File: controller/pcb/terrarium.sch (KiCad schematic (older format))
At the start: 54 parts, among them Q1 S8050, Q2 S8050, Q3 S8050, SW1 SW_Push, SW2 SW_Push, U1 ESP32-WROOM-32, U2 DS3231M, U3 LM1117-3.3

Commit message: pcb: developing smd layout
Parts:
- D1, D2, D3: footprint Diode_THT:D_DO-41_SOD81_P7.62mm_Horizontal -> Diode_SMD:D_1206_3216Metric
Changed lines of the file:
@@
 F 0 "D1" V 7350 1600 50  0000 L CNN
 F 1 "1N47xxA" H 7200 1450 50  0000 L CNN
-F 2 "Diode_THT:D_DO-41_SOD81_P7.62mm_Horizontal" H 7350 1375 50  0001 C CNN
+F 2 "Diode_SMD:D_1206_3216Metric" H 7350 1375 50  0001 C CNN
 F 3 "https://www.vishay.com/docs/85816/1n4728a.pdf" H 7350 1550 50  0001 C CNN
 	1    7350 1550
@@
 F 0 "D2" V 7350 3200 50  0000 L CNN
 F 1 "1N47xxA" H 7200 3050 50  0000 L CNN
-F 2 "Diode_THT:D_DO-41_SOD81_P7.62mm_Horizontal" H 7350 2975 50  0001 C CNN
+F 2 "Diode_SMD:D_1206_3216Metric" H 7350 2975 50  0001 C CNN
 F 3 "https://www.vishay.com/docs/85816/1n4728a.pdf" H 7350 3150 50  0001 C CNN
 	1    7350 3150
@@
 F 0 "D3" V 7350 4750 50  0000 L CNN
 F 1 "1N47xxA" H 7200 4600 50  0000 L CNN
-F 2 "Diode_THT:D_DO-41_SOD81_P7.62mm_Horizontal" H 7350 4525 50  0001 C CNN
+F 2 "Diode_SMD:D_1206_3216Metric" H 7350 4525 50  0001 C CNN
 F 3 "https://www.vishay.com/docs/85816/1n4728a.pdf" H 7350 4700 50  0001 C CNN
 	1    7350 4700

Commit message: Add copper plate, minor changes
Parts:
- H1, H2, H3, H4: footprint MountingHole:MountingHole_3.2mm_M3_DIN965_Pad -> MountingHole:MountingHole_3.2mm_M3_Pad_Via
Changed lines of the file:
@@
 F 0 "H1" H 3500 3500 50  0000 L CNN
 F 1 "MountingHole" H 3500 3455 50  0001 L CNN
-F 2 "MountingHole:MountingHole_3.2mm_M3_DIN965_Pad" H 3400 3500 50  0001 C CNN
+F 2 "MountingHole:MountingHole_3.2mm_M3_Pad_Via" H 3400 3500 50  0001 C CNN
 F 3 "~" H 3400 3500 50  0001 C CNN
 	1    3400 3500
@@
 F 0 "H2" H 3900 3500 50  0000 L CNN
 F 1 "MountingHole" H 3900 3455 50  0001 L CNN
-F 2 "MountingHole:MountingHole_3.2mm_M3_DIN965_Pad" H 3800 3500 50  0001 C CNN
+F 2 "MountingHole:MountingHole_3.2mm_M3_Pad_Via" H 3800 3500 50  0001 C CNN
 F 3 "~" H 3800 3500 50  0001 C CNN
 	1    3800 3500
@@
 F 0 "H3" H 3500 3800 50  0000 L CNN
 F 1 "MountingHole" H 3500 3755 50  0001 L CNN
-F 2 "MountingHole:MountingHole_3.2mm_M3_DIN965_Pad" H 3400 3800 50  0001 C CNN
+F 2 "MountingHole:MountingHole_3.2mm_M3_Pad_Via" H 3400 3800 50  0001 C CNN
 F 3 "~" H 3400 3800 50  0001 C CNN
 	1    3400 3800
@@
 F 0 "H4" H 3900 3800 50  0000 L CNN
 F 1 "MountingHole" H 3900 3755 50  0001 L CNN
-F 2 "MountingHole:MountingHole_3.2mm_M3_DIN965_Pad" H 3800 3800 50  0001 C CNN
+F 2 "MountingHole:MountingHole_3.2mm_M3_Pad_Via" H 3800 3800 50  0001 C CNN
 F 3 "~" H 3800 3800 50  0001 C CNN
 	1    3800 3800

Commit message: pcb updates
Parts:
- SW1: value SW_Push -> RESET
- SW2: value SW_Push -> BOOT
- renumbered CONN1 to UART1
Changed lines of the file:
@@
 P 14950 1600
 F 0 "SW2" H 14950 1885 50  0000 C CNN
-F 1 "SW_Push" H 14950 1794 50  0000 C CNN
+F 1 "BOOT" H 14950 1794 50  0000 C CNN
 F 2 "Button_Switch_SMD:SW_DIP_SPSTx01_Slide_6.7x4.1mm_W6.73mm_P2.54mm_LowProfile_JPin" H 14950 1800 50  0001 C CNN
 F 3 "~" H 14950 1800 50  0001 C CNN
@@
 P 11950 1600
 F 0 "SW1" H 11950 1885 50  0000 C CNN
-F 1 "SW_Push" H 11950 1794 50  0000 C CNN
+F 1 "RESET" H 11950 1794 50  0000 C CNN
 F 2 "Button_Switch_SMD:SW_DIP_SPSTx01_Slide_6.7x4.1mm_W6.73mm_P2.54mm_LowProfile_JPin" H 11950 1800 50  0001 C CNN
 F 3 "~" H 11950 1800 50  0001 C CNN
@@
 $EndComp
 $Comp
-L Connector_Generic:Conn_01x04 CONN1
+L Connector_Generic:Conn_01x04 UART1
 U 1 1 61BD0ED7
 P 12500 3700
-F 0 "CONN1" H 12580 3692 50  0000 L CNN
-F 1 "data" H 12580 3601 50  0000 L CNN
+F 0 "UART1" H 12580 3692 50  0000 L CNN
+F 1 "data" H 12650 3100 50  0001 L CNN
 F 2 "Connector_PinHeader_2.54mm:PinHeader_1x04_P2.54mm_Vertical" H 12500 3700 50  0001 C CNN
 F 3 "~" H 12500 3700 50  0001 C CNN

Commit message: pcb: updates
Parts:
- added D4: 1N47xxA, Diode_SMD:D_1206_3216Metric, symbol Diode:1N47xxA
- added SW3: RESET RTC, Button_Switch_SMD:SW_DIP_SPSTx01_Slide_6.7x4.1mm_W6.73mm_P2.54mm_LowProfile_JPin, symbol Switch:SW_Push
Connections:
- wire segments 169 -> 171
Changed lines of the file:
@@
 $EndComp
 Wire Wire Line
-	3250 8300 3250 7800
-Wire Wire Line
-	2350 7800 3250 7800
+	3250 8300 3250 8250
+Wire Wire Line
+	2350 7800 2650 7800
 Wire Wire Line
 	3250 8600 3250 9050
@@
 	1    0    0    -1
 $EndComp
+$Comp
+L Diode:1N47xxA D4
+U 1 1 61C05BEB
+P 2800 7800
+F 0 "D4" H 2750 7900 50  0000 L CNN
+F 1 "1N47xxA" H 2650 7700 50  0000 L CNN
+F 2 "Diode_SMD:D_1206_3216Metric" H 2800 7625 50  0001 C CNN
+F 3 "https://www.vishay.com/docs/85816/1n4728a.pdf" H 2800 7800 50  0001 C CNN
+	1    2800 7800
+	1    0    0    -1
+$EndComp
+Wire Wire Line
+	2950 7800 3250 7800
+$Comp
+L Switch:SW_Push SW3
+U 1 1 61C4BD91
+P 3250 8050
+F 0 "SW3" H 3250 8335 50  0000 C CNN
+F 1 "RESET RTC" H 3250 8244 50  0000 C CNN
+F 2 "Button_Switch_SMD:SW_DIP_SPSTx01_Slide_6.7x4.1mm_W6.73mm_P2.54mm_LowProfile_JPin" H 3250 8250 50  0001 C CNN
+F 3 "~" H 3250 8250 50  0001 C CNN
+	1    3250 8050
+	0    1    1    0
+$EndComp
+Wire Wire Line
+	3250 7850 3250 7800
 $EndSCHEMATC

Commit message: pcb v1.3 finished
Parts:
- D1, D2, D3: value 1N47xxA -> M7; footprint Diode_SMD:D_1206_3216Metric -> Diode_SMD:D_2114_3652Metric
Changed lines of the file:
@@
 P 7350 1550
 F 0 "D1" V 7350 1600 50  0000 L CNN
-F 1 "1N47xxA" H 7200 1450 50  0000 L CNN
-F 2 "Diode_SMD:D_1206_3216Metric" H 7350 1375 50  0001 C CNN
+F 1 "M7" V 7350 1350 50  0000 L CNN
+F 2 "Diode_SMD:D_2114_3652Metric" H 7350 1375 50  0001 C CNN
 F 3 "https://www.vishay.com/docs/85816/1n4728a.pdf" H 7350 1550 50  0001 C CNN
 	1    7350 1550
@@
 P 7350 3150
 F 0 "D2" V 7350 3200 50  0000 L CNN
-F 1 "1N47xxA" H 7200 3050 50  0000 L CNN
-F 2 "Diode_SMD:D_1206_3216Metric" H 7350 2975 50  0001 C CNN
+F 1 "M7" V 7350 2950 50  0000 L CNN
+F 2 "Diode_SMD:D_2114_3652Metric" H 7350 2975 50  0001 C CNN
 F 3 "https://www.vishay.com/docs/85816/1n4728a.pdf" H 7350 3150 50  0001 C CNN
 	1    7350 3150
@@
 P 7350 4700
 F 0 "D3" V 7350 4750 50  0000 L CNN
-F 1 "1N47xxA" H 7200 4600 50  0000 L CNN
-F 2 "Diode_SMD:D_1206_3216Metric" H 7350 4525 50  0001 C CNN
+F 1 "M7" V 7350 4500 50  0000 L CNN
+F 2 "Diode_SMD:D_2114_3652Metric" H 7350 4525 50  0001 C CNN
 F 3 "https://www.vishay.com/docs/85816/1n4728a.pdf" H 7350 4700 50  0001 C CNN
 	1    7350 4700

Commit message: Pcb/v1.4 (#3)
* pcb: refactor

* minor updates, bjt to sot-23

* rtc charge, refactoring

* update jst footprints, added missing 3d models

* refactoring

* minor changes

* diode for battery

* fix bugs in UART

* add transistor for sensors

* move status led from relay circuit

* pcb v1.4 release

* fix snake logo

Co-authored-by: Grigorii Merkushev <brushknight@pop-os.localdomain>
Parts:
- removed Q1, Q2: S8050, Package_TO_SOT_THT:TO-92_Inline, symbol Transistor_BJT:S8050
- removed SW2: BOOT, Button_Switch_SMD:SW_DIP_SPSTx01_Slide_6.7x4.1mm_W6.73mm_P2.54mm_LowProfile_JPin, symbol Switch:SW_Push
- added LED5: SENS, LED_SMD:LED_1206_3216Metric, symbol Device:LED
- added Q1, Q2, Q4: S8050, Package_TO_SOT_SMD:SOT-23, symbol Device:Q_NPN_BEC
- added R13: 100k, Resistor_SMD:R_1206_3216Metric, symbol Device:R_Small
- added R14, R15, R16, R17: 5k, Resistor_SMD:R_1206_3216Metric, symbol Device:R_Small
- added RESET_j1: data, Connector_PinHeader_2.54mm:PinHeader_1x02_P2.54mm_Vertical, symbol Connector_Generic:Conn_01x02
- added TP1, TP2: TestPoint, TestPoint:TestPoint_Pad_1.5x1.5mm, symbol Connector:TestPoint
- D1, D2, D3: footprint Diode_SMD:D_2114_3652Metric -> Diode_SMD:D_2010_5025Metric
- D4: footprint Diode_SMD:D_1206_3216Metric -> Diode_SMD:D_2010_5025Metric
- Q3: footprint Package_TO_SOT_THT:TO-92_Inline -> Package_TO_SOT_SMD:SOT-23; symbol Transistor_BJT:S8050 -> Device:Q_NPN_BEC
- R10: value 10k -> 150ohm
- R12: value 300 -> 5k
- R2, R4, R6: value R_Small -> 10
- SW3: value RESET RTC -> RTC BATTERY
- UART1: footprint Connector_PinHeader_2.54mm:PinHeader_1x04_P2.54mm_Vertical -> Connector_PinHeader_2.54mm:PinHeader_1x06_P2.54mm_Vertical; symbol Connector_Generic:Conn_01x04 -> Connector_Generic:Conn_01x06
- renumbered HT1 to SENS1, HT2 to SENS2, HT3 to SENS3, HT4 to SENS4, HT5 to SENS5, HT6 to SENS6
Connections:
- net labels added: EN, G32, G33, IO0
- wire segments 171 -> 192
- no-connect marks 30 -> 28
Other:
- note added: "DS3231 rtc"
- note added: "ESP32 WROOM 32"
- note added: "Power 3v3 and 5v"
- note added: "Sensors"
- note added: "Status LED"
- note removed: "DHT22 sensors"
- note removed: "Utils"
- moved on the sheet: ALED1, BT1, C1, C2, C3, D1, D2, D3, D4, H1, H2, H3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

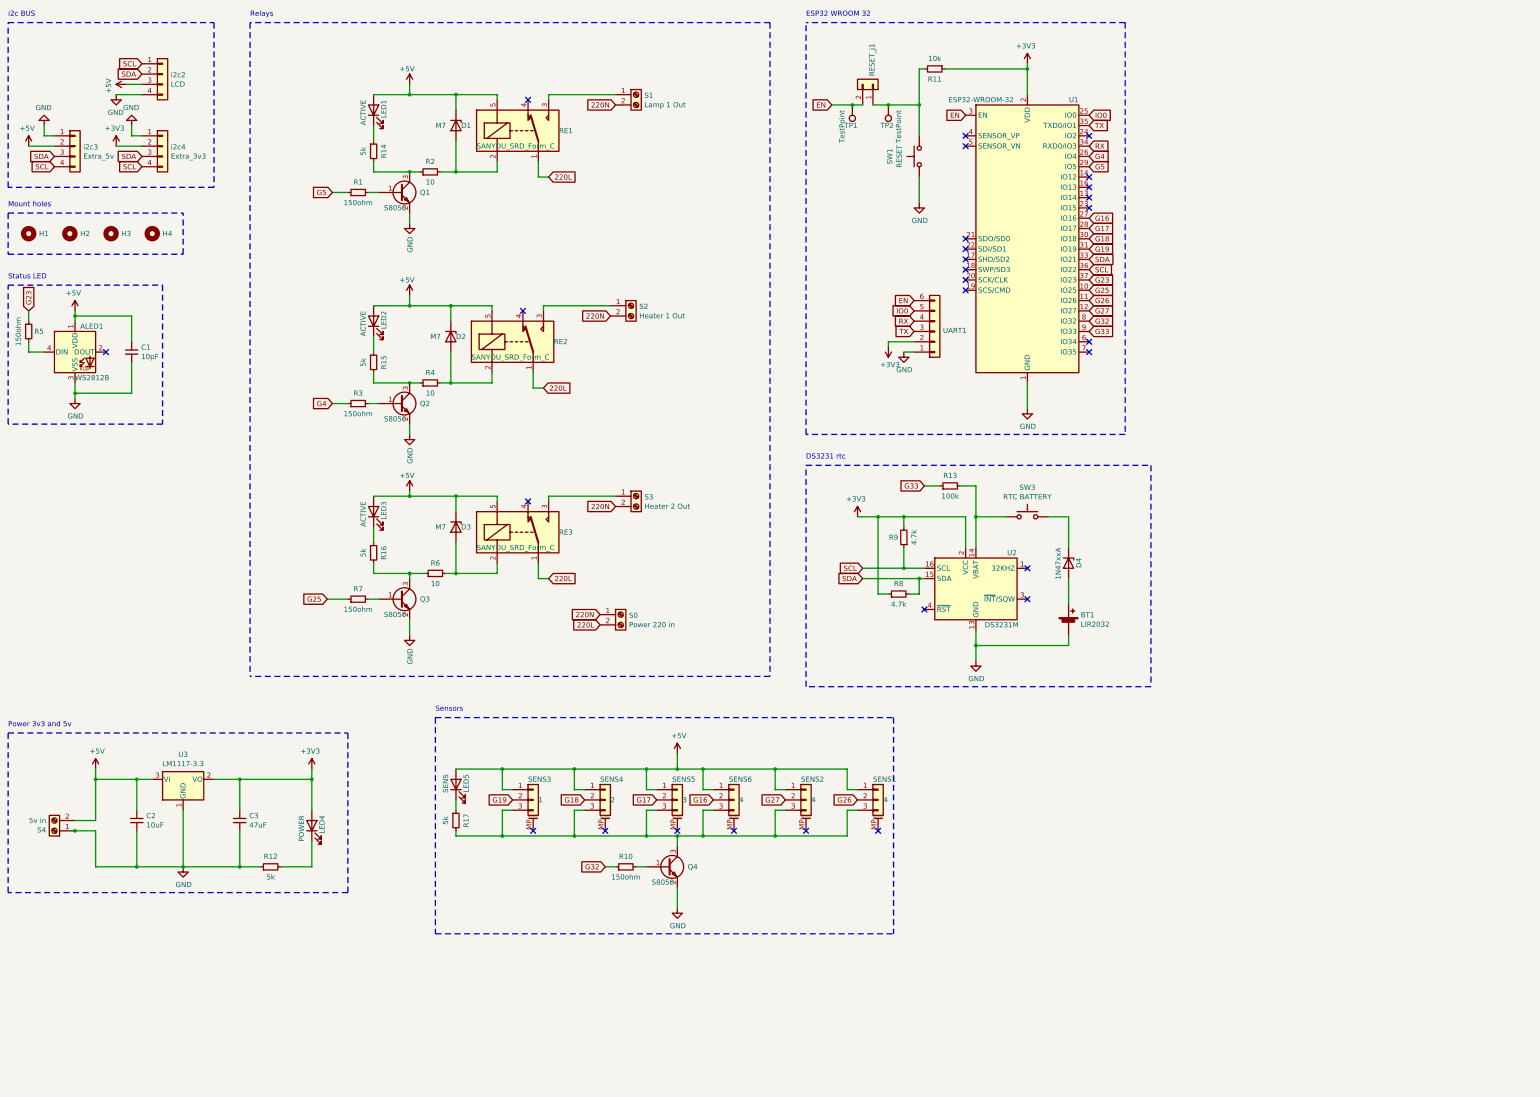
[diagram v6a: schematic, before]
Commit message: Controller pcb/v1.6 (#4)
* working on pcb/1v1.5

* wip, added all footprints

* place components for v1.5

* almost done

* update footprints, move rx/tx leds

* add cp2102

* add ground, 5v inner planes

* add multiplexer for i2c, rearrange everything

* fix CP2102, minor bugs

* minor updates for cp2102

* feat: add 5 pin sensor connectors

* wip qnfp28

* rearrange components

* fix bugs, update button footprint

* update ssr circuits

* release

Co-authored-by: Grigorii Merkushev <brushknight@pop-os.localdomain>
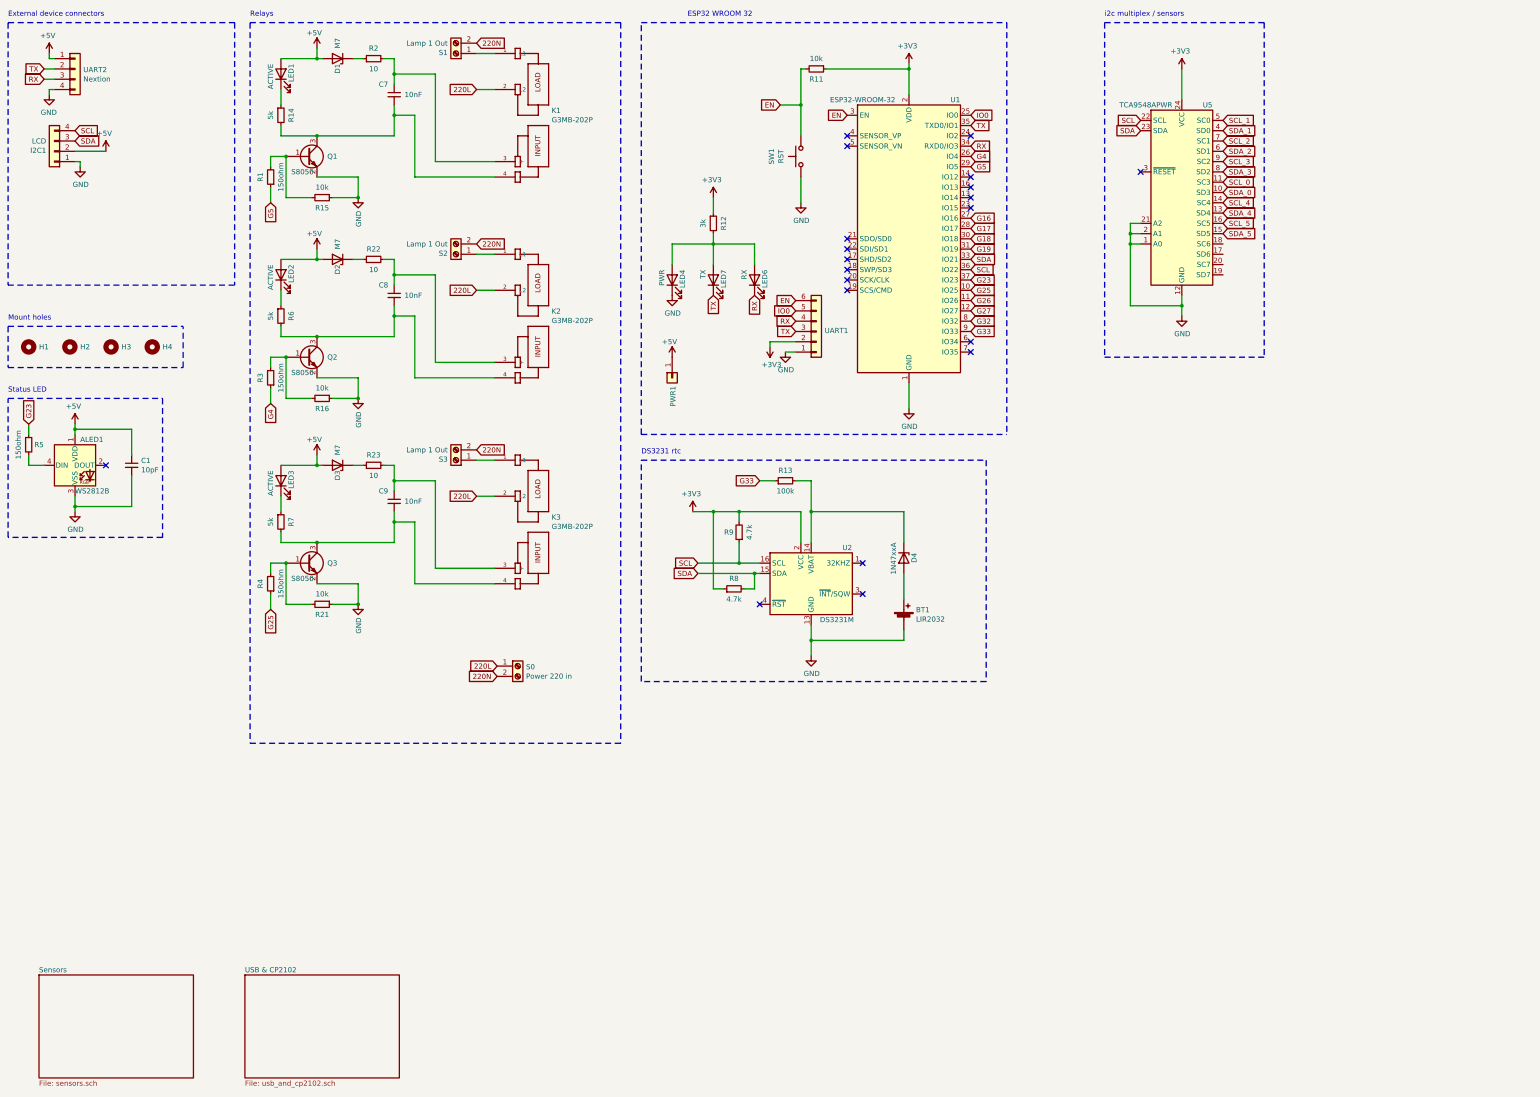
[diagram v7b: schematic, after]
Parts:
- removed C2: 10uF, Capacitor_SMD:C_1206_3216Metric, symbol Device:C_Small
- removed C3: 47uF, Capacitor_SMD:C_1206_3216Metric, symbol Device:C_Small
- removed LED5: SENS, LED_SMD:LED_1206_3216Metric, symbol Device:LED
- removed Q4: S8050, Package_TO_SOT_SMD:SOT-23, symbol Device:Q_NPN_BEC
- removed R10: 150ohm, Resistor_SMD:R_1206_3216Metric, symbol Device:R_Small
- removed R17: 5k, Resistor_SMD:R_1206_3216Metric, symbol Device:R_Small
- removed RE1, RE2, RE3: SANYOU_SRD_Form_C, Relay_THT:Relay_SPDT_SANYOU_SRD_Series_Form_C, symbol Relay:SANYOU_SRD_Form_C
- removed RESET_j1: data, Connector_PinHeader_2.54mm:PinHeader_1x02_P2.54mm_Vertical, symbol Connector_Generic:Conn_01x02
- removed S4: 5v in, TerminalBlock:TerminalBlock_bornier-2_P5.08mm, symbol Connector:Screw_Terminal_01x02
- removed SENS1, SENS2, SENS6: 4, Connector_JST:JST_XH_B3B-XH-AM_1x03_P2.50mm_Vertical, symbol Connector_Generic_MountingPin:Conn_01x03_MountingPin
- removed SENS3: 1, Connector_JST:JST_XH_B3B-XH-AM_1x03_P2.50mm_Vertical, symbol Connector_Generic_MountingPin:Conn_01x03_MountingPin
- removed SENS4: 2, Connector_JST:JST_XH_B3B-XH-AM_1x03_P2.50mm_Vertical, symbol Connector_Generic_MountingPin:Conn_01x03_MountingPin
- removed SENS5: 3, Connector_JST:JST_XH_B3B-XH-AM_1x03_P2.50mm_Vertical, symbol Connector_Generic_MountingPin:Conn_01x03_MountingPin
- removed SW3: RTC BATTERY, Button_Switch_SMD:SW_DIP_SPSTx01_Slide_6.7x4.1mm_W6.73mm_P2.54mm_LowProfile_JPin, symbol Switch:SW_Push
- removed TP1, TP2: TestPoint, TestPoint:TestPoint_Pad_1.5x1.5mm, symbol Connector:TestPoint
- removed U3: LM1117-3.3, Package_TO_SOT_SMD:SOT-223-3_TabPin2, symbol Regulator_Linear:LM1117-3.3
- removed i2c2: LCD, Connector_JST:JST_XH_B4B-XH-AM_1x04_P2.50mm_Vertical, symbol Connector_Generic:Conn_01x04
- removed i2c3: Extra_5v, Connector_PinHeader_2.54mm:PinHeader_1x04_P2.54mm_Vertical, symbol Connector_Generic:Conn_01x04
- removed i2c4: Extra_3v3, Connector_PinHeader_2.54mm:PinHeader_1x04_P2.54mm_Vertical, symbol Connector_Generic:Conn_01x04
- added C7, C8, C9: 10nF, Capacitor_SMD:C_1206_3216Metric, symbol Device:C_Small
- added I2C1: LCD, Connector_JST:JST_XH_B4B-XH-AM_1x04_P2.50mm_Vertical, symbol Connector_Generic:Conn_01x04
- added K1, K2, K3: G3MB-202P, omron:RELAY_G3MB-202P, symbol terrarium-rescue:G3MB-202P-G3MB-202P
- added LED6: RX, LED_SMD:LED_1206_3216Metric, symbol Device:LED
- added LED7: TX, LED_SMD:LED_1206_3216Metric, symbol Device:LED
- added PWR1: data, Connector_PinHeader_2.54mm:PinHeader_1x01_P2.54mm_Vertical, symbol Connector_Generic:Conn_01x01
- added R21: 10k, Resistor_SMD:R_1206_3216Metric, symbol Device:R_Small
- added R22, R23: 10, Resistor_SMD:R_1206_3216Metric, symbol Device:R_Small
- added U5: TCA9548APWR, Package_SO:TSSOP-24_4.4x7.8mm_P0.65mm, symbol Interface_Expansion:TCA9548APWR
- added UART2: Nextion, Connector_JST:JST_XH_B4B-XH-AM_1x04_P2.50mm_Vertical, symbol Connector_Generic:Conn_01x04
- BT1: footprint Battery:BatteryHolder_Keystone_1058_1x2032 -> Custom_Battery:CR2032_vertical
- LED4: value POWER -> PWR
- R12: value 5k -> 3k
- R15, R16: value 5k -> 10k
- R4: value 10 -> 150ohm
- R6: value 10 -> 5k
- R7: value 150ohm -> 5k
- S2: value Heater 1 Out -> Lamp 1 Out
- S3: value Heater 2 Out -> Lamp 1 Out
- SW1: value RESET -> RST; footprint Button_Switch_SMD:SW_DIP_SPSTx01_Slide_6.7x4.1mm_W6.73mm_P2.54mm_LowProfile_JPin -> Button_Switch_THT:SW_Tactile_SPST_Angled_PTS645Vx39-2LFS
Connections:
- net +3V3: now also R12.1, U5.24 (VCC); no longer LED4.2 (A)
- net +5V: now also D1.2 (A), D2.2 (A), D3.2 (A), I2C1.2 (Pin_2), PWR1.1 (Pin_1), UART2.1 (Pin_1); no longer D1.1 (K), D2.1 (K), D3.1 (K)
- net 220L: now also S0.1 (Pin_1), K1.2 (L2), K2.2 (L2), K3.2 (L2); no longer S0.2 (Pin_2)
- net 220N: now also S0.2 (Pin_2); no longer S0.1 (Pin_1)
- net EN: now also R11.2, SW1.2
- net G25: now also R4.1; no longer R7.1
- net GND: now also LED4.1 (K), R15.1, R16.1, I2C1.1 (Pin_1), R21.1, U5.1 (A0), U5.12 (GND), U5.2 (A1), U5.21 (A2), UART2.4 (Pin_4); no longer R12.1
- net RX: now also LED6.1 (K), UART2.3 (Pin_3)
- net SCL: now also I2C1.4 (Pin_4), U5.22 (SCL)
- net SDA: now also I2C1.3 (Pin_3), U5.23 (SDA)
- net TX: now also LED7.1 (K), UART2.2 (Pin_2)
- net at R4.2: now also Q3.1 (B), R21.2; no longer D2.2 (A)
- net at Q1.3 (C), R14.2: now also C7.2, K1.4 (-); no longer R2.1
- net at R2.2: now also C7.1, K1.3 (+); no longer D1.2 (A)
- net at Q1.1 (B), R1.2: now also R15.2
- net at S1.1 (Pin_1): now also K1.1 (L1)
- net at S2.1 (Pin_1): now also K2.1 (L1)
- net at R13.2, U2.14 (VBAT): now also D4.1 (K)
- net at Q2.1 (B), R3.2: now also R16.2
- net at LED2.1 (K): now also R6.1; no longer R15.1
- net at R7.2: now also Q3.3 (C), C9.2, K3.4 (-); no longer Q3.1 (B)
- net at LED3.1 (K): now also R7.1; no longer R16.1
- net at R6.2: now also Q2.3 (C), C8.2, K2.4 (-); no longer D3.2 (A)
- net at S3.1 (Pin_1): now also K3.1 (L1)
- net at R12.2: now also LED4.2 (A), LED6.2 (A), LED7.2 (A); no longer LED4.1 (K)
- new net: D1.1 (K), R2.1
- new net: C8.1, K2.3 (+), R22.2
- new net: D2.1 (K), R22.1
- new net: C9.1, K3.3 (+), R23.2
- new net: D3.1 (K), R23.1
- new net SCL_0: U5.11 (SC3)
- new net SCL_1: U5.5 (SC0)
- new net SCL_2: U5.7 (SC1)
- new net SCL_3: U5.9 (SC2)
- new net SCL_4: U5.14 (SC4)
- new net SCL_5: U5.16 (SC5)
- new net SDA_0: U5.10 (SD3)
- new net SDA_1: U5.4 (SD0)
- new net SDA_2: U5.6 (SD1)
- new net SDA_3: U5.8 (SD2)
- new net SDA_4: U5.13 (SD4)
- new net SDA_5: U5.15 (SD5)
- no-connect marks 28 -> 20
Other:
- note added: "External device connectors"
- note added: "i2c multiplex / sensors"
- note removed: "Power 3v3 and 5v"
- note removed: "Sensors"
- note removed: "i2c BUS"
- moved on the sheet: ALED1, BT1, C1, D1, D4, H1, H2, H3, H4, LED1, LED4, Q1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
